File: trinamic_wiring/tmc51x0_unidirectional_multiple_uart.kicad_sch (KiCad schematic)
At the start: 2 parts

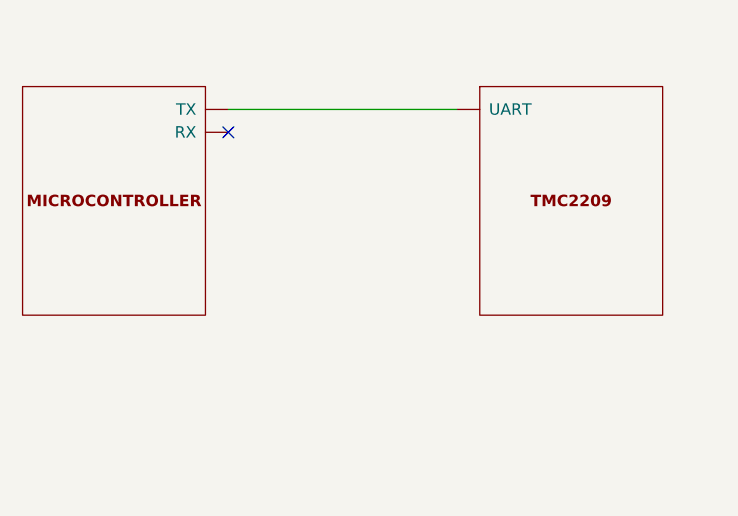
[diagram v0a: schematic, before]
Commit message: Add TMC51X0 files
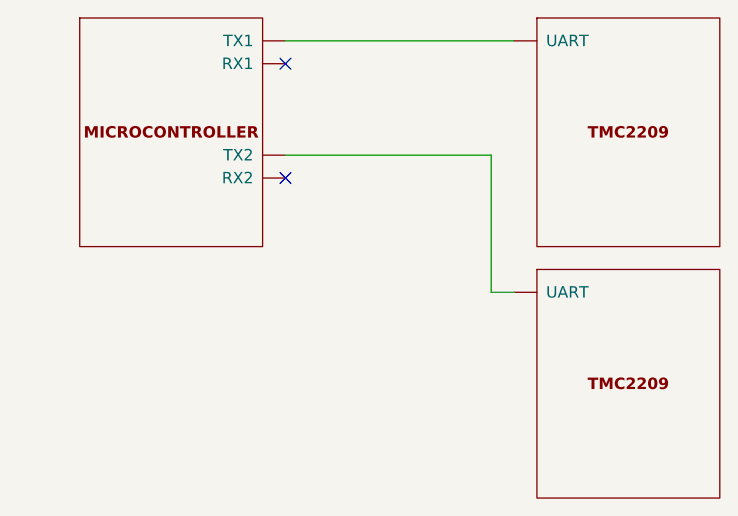
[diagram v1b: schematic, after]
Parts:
- removed MICROCONTROLLER4: DOC_MCU, symbol Janelia:DOC_MCU
- removed TMC6: DOC_TMC2209, symbol Janelia:DOC_TMC2209
- added MICROCONTROLLER6: DOC_MCU, symbol Janelia:DOC_MCU
- added TMC10, TMC9: DOC_TMC2209, symbol Janelia:DOC_TMC2209
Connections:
- new net: MICROCONTROLLER6.1 (TX1), TMC9.0 (UART)
- new net: MICROCONTROLLER6.3 (TX2), TMC10.0 (UART)
- no-connect marks 1 -> 2
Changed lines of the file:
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@@
     (company "Janelia Research Campus")
   )
-  (no_connect (at 119.38 87.63))
-  (wire (pts (xy 119.38 85.09) (xy 144.78 85.09))
+  (no_connect (at 125.73 80.01))
+  (no_connect (at 125.73 92.71))
+  (wire (pts (xy 125.73 77.47) (xy 151.13 77.47))
     (stroke (width 0) (type default))
   )
-  (symbol (lib_id "Janelia:DOC_MCU") (at 106.68 95.25 0) (unit 1)
+  (wire (pts (xy 148.59 90.17) (xy 148.59 105.41))
+    (stroke (width 0) (type default))
+  )
+  (wire (pts (xy 148.59 105.41) (xy 151.13 105.41))
+    (stroke (width 0) (type default))
+  )
+  (wire (pts (xy 125.73 90.17) (xy 148.59 90.17))
+    (stroke (width 0) (type default))
+  )
+  (symbol (lib_id "Janelia:DOC_MCU") (at 113.03 87.63 0) (unit 1)
     (in_bom yes) (on_board yes) (dnp no) (fields_autoplaced)
-    (property "Reference" "MICROCONTROLLER4" (at 106.68 76.2 0)
+    (property "Reference" "MICROCONTROLLER6" (at 113.03 68.58 0)
       (effects (font (size 1.27 1.27)) hide)
     )
-    (property "Value" "DOC_MCU" (at 106.68 81.28 0)
+    (property "Value" "DOC_MCU" (at 113.03 73.66 0)
       (effects (font (size 1.524 1.524)) hide)
     )
-    (property "Footprint" "" (at 104.14 121.92 0)
+    (property "Footprint" "" (at 110.49 114.3 0)
       (effects (font (size 1.524 1.524)) hide)
     )
-    (property "Datasheet" "" (at 106.68 95.25 0)
+    (property "Datasheet" "" (at 113.03 87.63 0)
       (effects (font (size 1.524 1.524)) hide)
     )
-    (property "Sim.Enable" "0" (at 106.68 78.74 0)
+    (property "Sim.Enable" "0" (at 113.03 71.12 0)
       (effects (font (size 1.27 1.27)) hide)
     )
@@
     (instances
       (project "trinamic_wiring"
-        (path "/e4144788-6304-493f-818e-5d881d3b7418/c8eda2b5-ab13-4033-82d9-875c9fcaf884/13e2a7b5-46df-44bb-8dde-5d79d190b8bf"
-          (reference "MICROCONTROLLER4") (unit 1)
+        (path "/e4144788-6304-493f-818e-5d881d3b7418/c8eda2b5-ab13-4033-82d9-875c9fcaf884/d4a56977-1958-4e49-bd54-bb12e595a31d"
+          (reference "MICROCONTROLLER6") (unit 1)
         )
-        (path "/e4144788-6304-493f-818e-5d881d3b7418/a161638e-a96f-4455-865a-1d7502675f43/13e2a7b5-46df-44bb-8dde-5d79d190b8bf"
-          (reference "MICROCONTROLLER4") (unit 1)
+        (path "/e4144788-6304-493f-818e-5d881d3b7418/a161638e-a96f-4455-865a-1d7502675f43/d4a56977-1958-4e49-bd54-bb12e595a31d"
+          (reference "MICROCONTROLLER6") (unit 1)
         )
       )
     )
   )
-  (symbol (lib_id "Janelia:DOC_TMC2209") (at 157.48 95.25 0) (unit 1)
+  (symbol (lib_id "Janelia:DOC_TMC2209") (at 163.83 87.63 0) (unit 1)
     (in_bom yes) (on_board yes) (dnp no) (fields_autoplaced)
-    (property "Reference" "TMC6" (at 157.48 76.2 0)
+    (property "Reference" "TMC9" (at 163.83 68.58 0)
       (effects (font (size 1.27 1.27)) hide)
     )
-    (property "Value" "DOC_TMC2209" (at 157.48 81.28 0)
+    (property "Value" "DOC_TMC2209" (at 163.83 73.66 0)
       (effects (font (size 1.524 1.524)) hide)
     )
-    (property "Footprint" "" (at 154.94 121.92 0)
+    (property "Footprint" "" (at 161.29 114.3 0)
       (effects (font (size 1.524 1.524)) hide)
     )
-    (property "Datasheet" "" (at 157.48 95.25 0)
+    (property "Datasheet" "" (at 163.83 87.63 0)
       (effects (font (size 1.524 1.524)) hide)
     )
-    (property "Sim.Enable" "0" (at 157.48 78.74 0)
+    (property "Sim.Enable" "0" (at 163.83 71.12 0)
       (effects (font (size 1.27 1.27)) hide)
     )
@@
     (instances
       (project "trinamic_wiring"
-        (path "/e4144788-6304-493f-818e-5d881d3b7418/c8eda2b5-ab13-4033-82d9-875c9fcaf884/13e2a7b5-46df-44bb-8dde-5d79d190b8bf"
-          (reference "TMC6") (unit 1)
+        (path "/e4144788-6304-493f-818e-5d881d3b7418/c8eda2b5-ab13-4033-82d9-875c9fcaf884/d4a56977-1958-4e49-bd54-bb12e595a31d"
+          (reference "TMC9") (unit 1)
         )
-        (path "/e4144788-6304-493f-818e-5d881d3b7418/a161638e-a96f-4455-865a-1d7502675f43/13e2a7b5-46df-44bb-8dde-5d79d190b8bf"
-          (reference "TMC6") (unit 1)
+        (path "/e4144788-6304-493f-818e-5d881d3b7418/a161638e-a96f-4455-865a-1d7502675f43/d4a56977-1958-4e49-bd54-bb12e595a31d"
+          (reference "TMC9") (unit 1)
         )
       )
+    )
+  )
+  (symbol (lib_id "Janelia:DOC_TMC2209") (at 163.83 115.57 0) (unit 1)
+    (in_bom yes) (on_board yes) (dnp no) (fields_autoplaced)
+    (property "Reference" "TMC10" (at 163.83 96.52 0)
+      (effects (font (size 1.27 1.27)) hide)
+    )
+    (property "Value" "DOC_TMC2209" (at 163.83 101.6 0)
+      (effects (font (size 1.524 1.524)) hide)
+    )
+    (property "Footprint" "" (at 161.29 142.24 0)
+      (effects (font (size 1.524 1.524)) hide)
+    )
+    (property "Datasheet" "" (at 163.83 115.57 0)
+      (effects (font (size 1.524 1.524)) hide)
+    )
+    (property "Sim.Enable" "0" (at 163.83 99.06 0)
+      (effects (font (size 1.27 1.27)) hide)
+    )
+    (pin "0")
+    (pin "1")
+    (pin "10")
+    (pin "2")
+    (pin "3")
+    (pin "4")
+    (pin "5")
+    (pin "6")
+    (pin "7")
+    (pin "8")
+    (pin "9")
+    (instances
+      (project "trinamic_wiring"
+        (path "/e4144788-6304-493f-818e-5d881d3b7418/c8eda2b5-ab13-4033-82d9-875c9fcaf884/d4a56977-1958-4e49-bd54-bb12e595a31d"
+          (reference "TMC10") (unit 1)
+        )
+        (path "/e4144788-6304-493f-818e-5d881d3b7418/a161638e-a96f-4455-865a-1d7502675f43/d4a56977-1958-4e49-bd54-bb12e595a31d"
+          (reference "TMC10") (unit 1)
+        )
+      )
